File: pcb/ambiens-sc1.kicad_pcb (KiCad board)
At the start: 4 copper layers, 80 x 80 mm, 119 parts, among them J1 AQ FAN, J10 AQ_SENSOR_0x77, J11 PWR_BTN, J12 CTRL, J13 BOOT1, J14 PROG, J15 Expansion, J2 Heater Temp, J3 Heater Fan, J4 AQ Fan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

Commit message: small fixes
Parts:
- moved C14 1.52 mm to (143.2, 113.7), turned to 180 degrees
- moved R18 1.15 mm to (143.1, 115.5), turned to 0 degrees
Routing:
- net /STM32/STM32_NRST: track 95.6 -> 90.1 mm
- net /STM32/PROG_SWD: track 27.9 -> 29.0 mm
- net /SCL_BUS: track 105.6 -> 106.6 mm
- net /STM32/PROG_SCLK: track 19.8 -> 19.2 mm

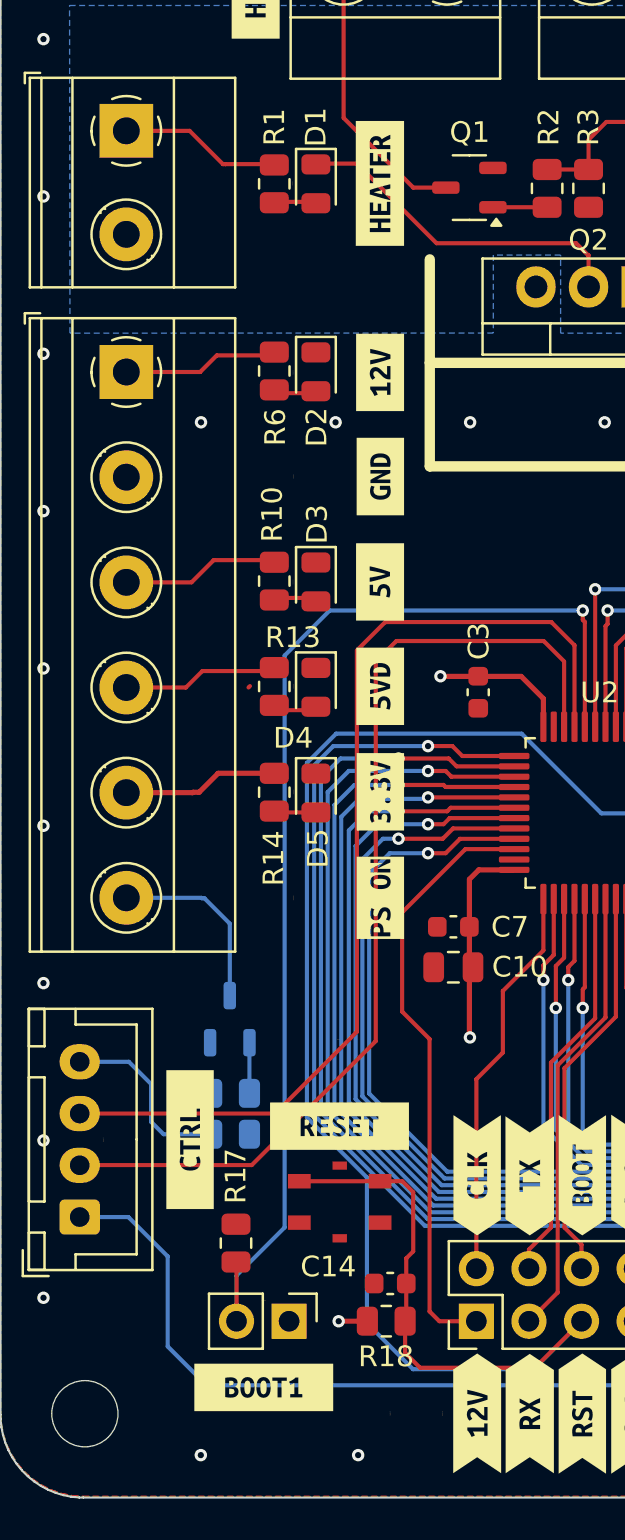
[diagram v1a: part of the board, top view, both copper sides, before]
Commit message: Fix red led + label typo
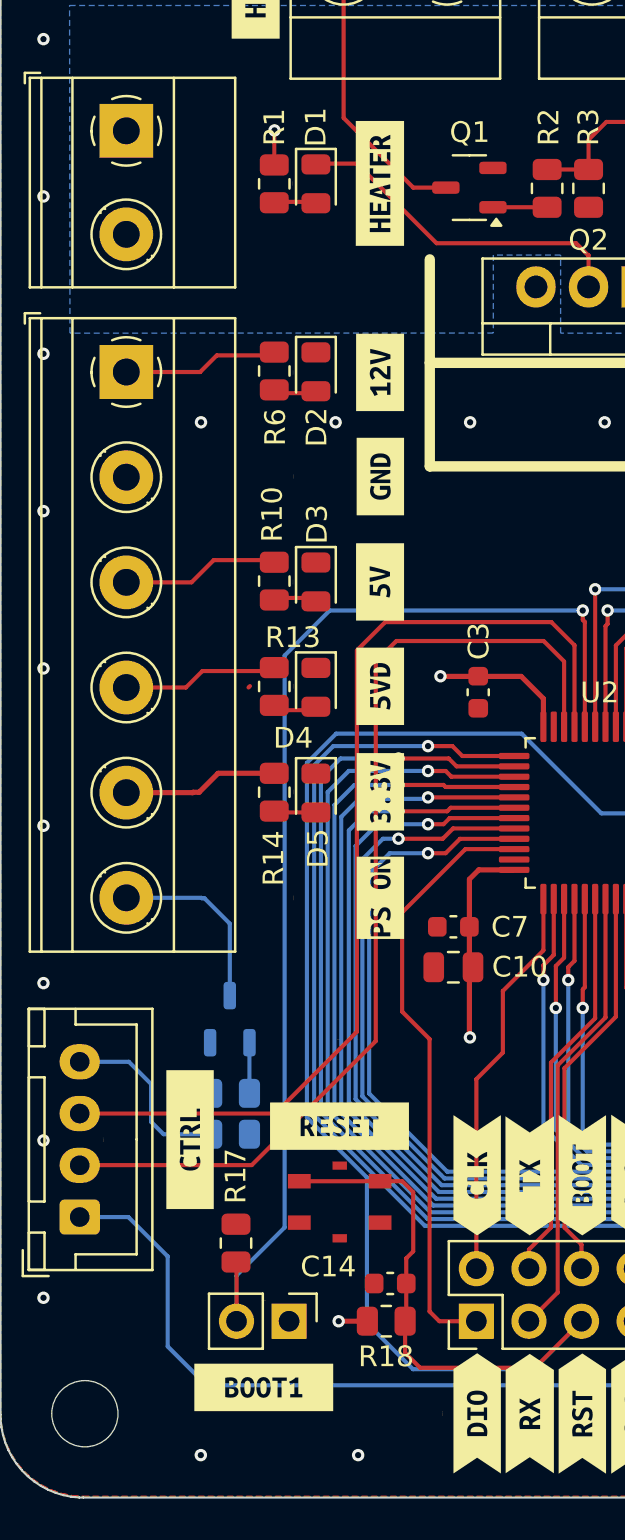
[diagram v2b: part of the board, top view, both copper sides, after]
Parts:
- removed kibuzzard-36: G***, kibuzzard-660B1ED2
- added kibuzzard-6634D528: G***, kibuzzard-6634D528, F.Cu at (147.4, 120.0)
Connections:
- R1 pad 1: Net-(D1-K) -> +12V
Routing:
- net Net-(D1-K): track 24.4 -> 16.5 mm
- net +12V: track 7.48 -> 9.15 mm, vias 0 -> 1
